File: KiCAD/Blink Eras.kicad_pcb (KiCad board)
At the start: 2 copper layers, 27.9 x 20.3 mm, 11 parts, among them IC1 ATTINY85-M, U1 ICM7555

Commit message: Hide passive component values.
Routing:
- net GND: track 2.79 -> 0.00 mm
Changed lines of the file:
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@@
     (thickness 1.6002)
     (drawings 8)
-    (tracks 73)
+    (tracks 71)
     (zones 0)
     (modules 11)
@@
   (page USLetter)
   (layers
-    (0 F.Cu signal hide)
+    (0 F.Cu signal)
     (31 B.Cu signal)
     (34 B.Paste user)
-    (35 F.Paste user hide)
+    (35 F.Paste user)
     (36 B.SilkS user)
-    (37 F.SilkS user hide)
+    (37 F.SilkS user)
     (38 B.Mask user)
-    (39 F.Mask user hide)
+    (39 F.Mask user)
     (44 Edge.Cuts user)
   )
@@
     (aux_axis_origin 0 0)
     (grid_origin 130.81 110.49)
-    (visible_elements FFFFFF7F)
+    (visible_elements FFFFFB7F)
     (pcbplotparams
       (layerselection 0x00030_80000001)
@@
       (effects (font (size 1 1) (thickness 0.15)))
     )
-    (fp_text value 1µ (at 0 1.9 270) (layer F.Fab)
+    (fp_text value 1µ (at 0 1.9 270) (layer F.Fab) hide
       (effects (font (size 1 1) (thickness 0.15)))
     )
@@
       (effects (font (size 1 1) (thickness 0.15)))
     )
-    (fp_text value Red (at 0 1.5 270) (layer F.Fab)
+    (fp_text value Red (at 0 1.5 270) (layer F.Fab) hide
       (effects (font (size 1 1) (thickness 0.15)))
     )
@@
       (effects (font (size 1 1) (thickness 0.15)))
     )
-    (fp_text value Green (at 0 1.5 270) (layer F.Fab)
+    (fp_text value Green (at 0 1.5 270) (layer F.Fab) hide
       (effects (font (size 1 1) (thickness 0.15)))
     )
@@
       (effects (font (size 1 1) (thickness 0.15)))
     )
-    (fp_text value 470K (at 0 1.9 90) (layer F.Fab)
+    (fp_text value 470K (at 0 1.9 90) (layer F.Fab) hide
       (effects (font (size 1 1) (thickness 0.15)))
     )
@@
       (effects (font (size 1 1) (thickness 0.15)))
     )
-    (fp_text value 68 (at 0 1.9 90) (layer F.Fab)
+    (fp_text value 68 (at 0 1.9 90) (layer F.Fab) hide
       (effects (font (size 1 1) (thickness 0.15)))
     )
@@
       (effects (font (size 1 1) (thickness 0.15)))
     )
-    (fp_text value 56 (at 0 1.9 270) (layer F.Fab)
+    (fp_text value 56 (at 0 1.9 270) (layer F.Fab) hide
       (effects (font (size 1 1) (thickness 0.15)))
     )
@@
   (segment (start 152.654 100.6) (end 155.31 100.6) (width 0.1524) (layer F.Cu) (net 1))
   (segment (start 155.31 100.6) (end 155.58 100.33) (width 0.1524) (layer F.Cu) (net 1))
-  (segment (start 144.78 100.33) (end 146.304 100.33) (width 0.1524) (layer B.Cu) (net 2))
-  (segment (start 146.304 100.33) (end 145.288 99.568) (width 0.1524) (layer B.Cu) (net 2))
   (via (at 145.288 99.568) (size 0.6858) (drill 0.3302) (layers F.Cu B.Cu) (net 2))
   (segment (start 137.16 107) (end 137.16 106.172) (width 0.1524) (layer F.Cu) (net 3))

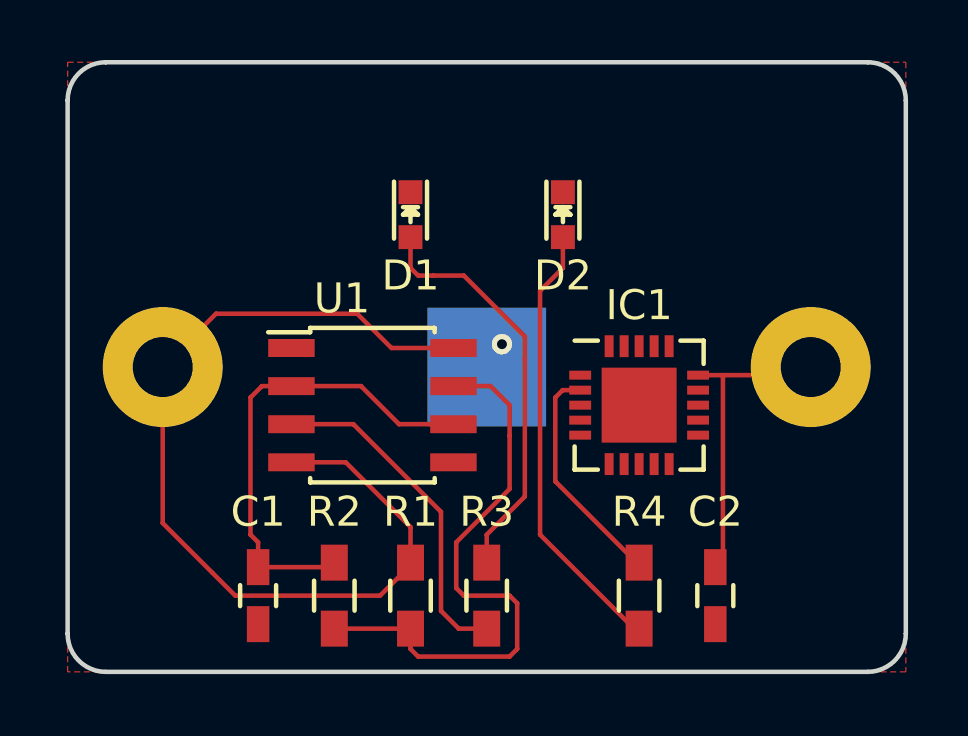
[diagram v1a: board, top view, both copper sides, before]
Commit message: New layout makes the pogo pins fit.
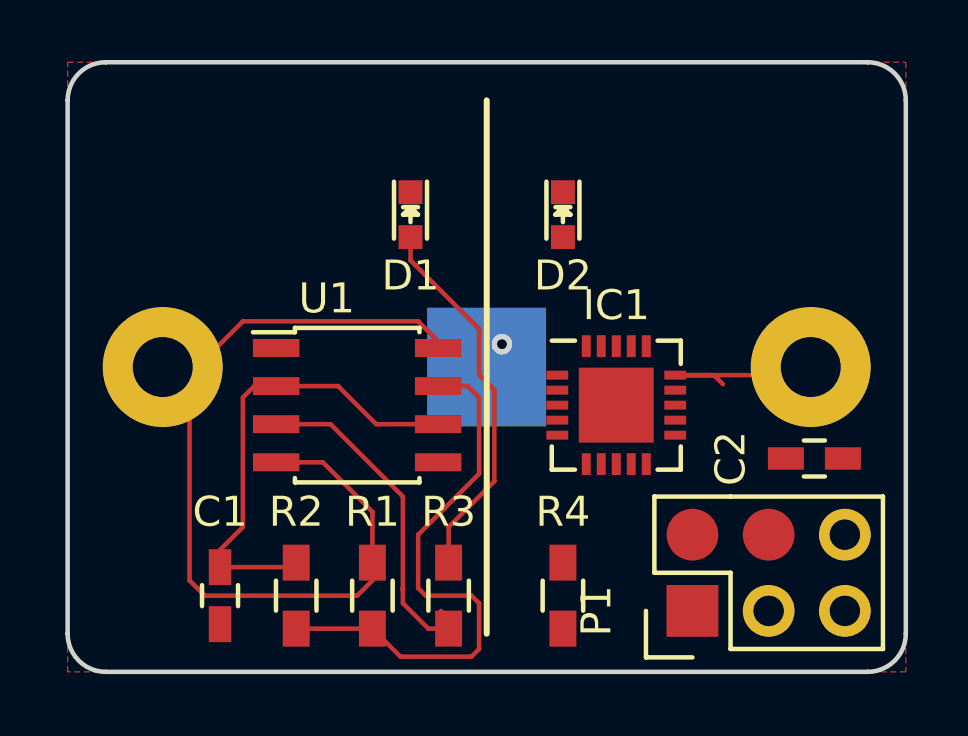
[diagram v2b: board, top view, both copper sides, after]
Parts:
- added P1: ISP, BlinkyFeet:ISP_Pogo_3-thru, F.Cu at (151.6, 108.5)
- moved C2 5.64 mm to (155.7, 103.4), turned to 0 degrees
- moved R4 2.54 mm to (147.3, 108.0)
- moved C1 1.27 mm to (135.9, 108.0)
- moved R1 1.27 mm to (141.0, 108.0)
- moved R3 1.27 mm to (143.5, 108.0)
- moved R2 1.27 mm to (138.4, 108.0)
- moved IC1 0.76 mm to (149.1, 101.6)
- moved U1 0.51 mm to (140.5, 101.6)
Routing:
- net Net-(D2-Pad2): track 14.8 -> 0.00 mm
- net Net-(IC1-Pad2): track 7.64 -> 0.07 mm
- net VCC: track 42.4 -> 37.0 mm
- net Net-(D1-Pad2): track 13.8 -> 12.6 mm
- net Net-(R1-Pad2): track 19.7 -> 19.1 mm
- net Net-(R3-Pad1): track 11.4 -> 12.1 mm

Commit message: Routed pogo pins.
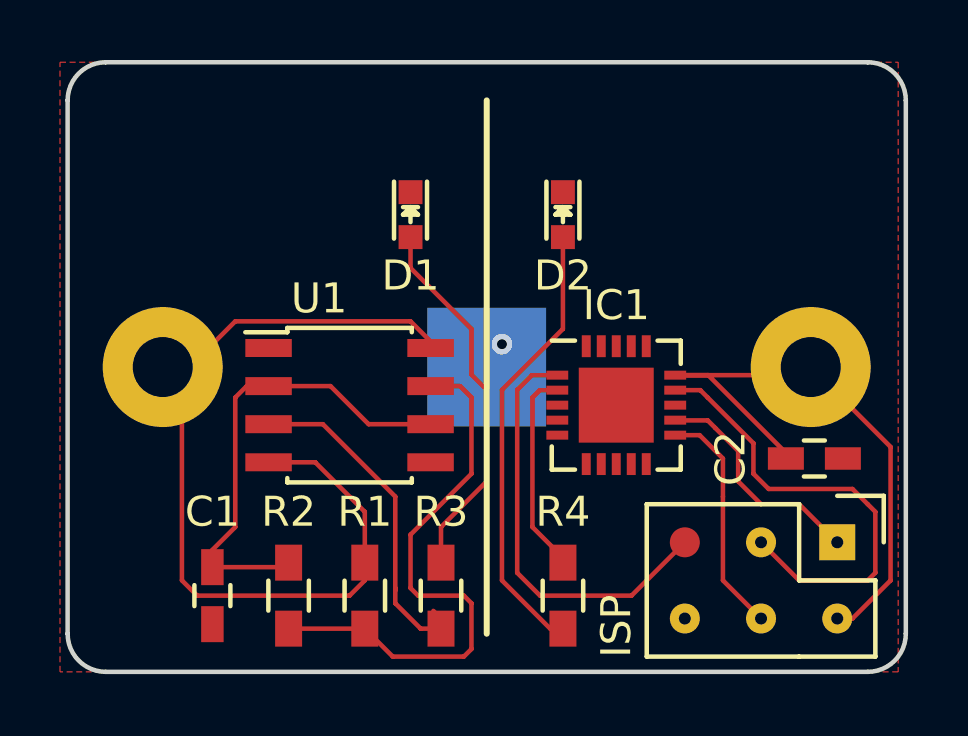
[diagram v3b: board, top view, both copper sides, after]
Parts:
- P1: footprint BlinkyFeet:ISP_Pogo_3-thru -> BlinkyFeet:ISP_Pogo_5-thru
- moved P1 5.34 mm to (156.5, 106.2), turned to 270 degrees
- moved R2 0.25 mm to (138.2, 108.0)
- moved C1 0.25 mm to (135.6, 108.0)
- moved R1 0.25 mm to (140.7, 108.0)
- moved R3 0.25 mm to (143.3, 108.0)
- moved U1 0.25 mm to (140.2, 101.6)
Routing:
- net /SCK: track 0.00 -> 15.4 mm
- net Net-(D2-Pad2): track 0.00 -> 15.0 mm
- net /~RESET~: track 0.00 -> 14.3 mm
- net VCC: track 37.0 -> 50.8 mm
- net /MISO: track 0.00 -> 7.95 mm
- net /MOSI: track 0.00 -> 7.77 mm
- net Net-(IC1-Pad2): track 0.07 -> 6.93 mm

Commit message: Tied QFN20's ground pad to ground.
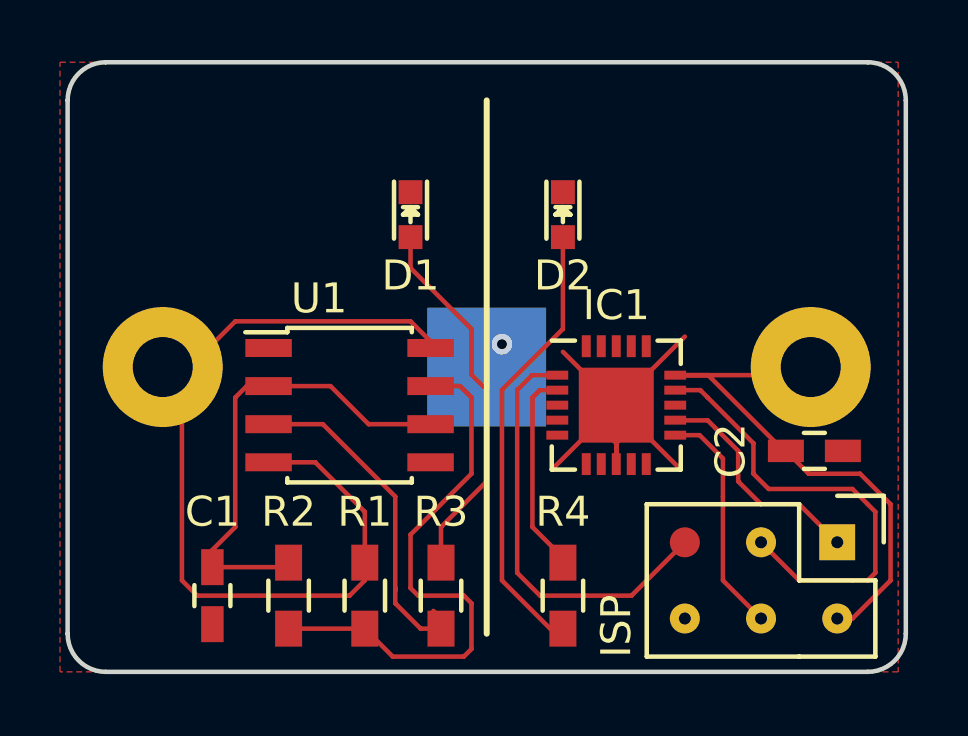
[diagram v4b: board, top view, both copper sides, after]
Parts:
- IC1: footprint Housings_DFN_QFN:QFN-20-1EP_4x4mm_Pitch0.5mm -> BlinkyFeet:QFN-20-1EP_4x4mm_Pitch0.5mm
- moved C2 0.25 mm to (155.7, 103.1)
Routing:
- net GND: track 0.00 -> 16.2 mm
- net VCC: track 50.8 -> 49.3 mm

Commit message: Big round battery contact, six vias to ground plane.
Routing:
- net GND: track 16.2 -> 60.8 mm, vias 1 -> 6
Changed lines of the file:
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@@
     (links 31)
     (no_connects 1)
-    (area 130.556 90.094999 158.825001 110.649401)
+    (area 130.556 90.0526 158.825001 110.649401)
     (thickness 1.6002)
     (drawings 9)
-    (tracks 129)
+    (tracks 153)
     (zones 0)
     (modules 12)
@@
     (add_net VCC)
   )
-  (module BlinkyFeet:BK-913 (layer B.Cu)
-    (at 144.78 100.33 180)
-    (fp_text reference BT1 (at 0 -8.89 180) (layer B.SilkS) hide
-      (effects (font (size 1 1) (thickness 0.15)) (justify mirror))
-    )
-    (fp_text value CR2032 (at 0 7.62 180) (layer B.SilkS)
-      (effects (font (size 1 1) (thickness 0.15)) (justify mirror))
-    )
-    (fp_circle (center 0 0) (end 10 0) (layer B.SilkS) (width 0.15))
-    (pad 1 thru_hole circle (at -10.8 0 180) (size 4 4) (drill 2) (layers *.Cu *.Mask B.SilkS)
-      (net 1 VCC))
-    (pad 2 smd rect (at 0 0 180) (size 3.96 3.96) (layers B.Cu B.Paste B.Mask)
-      (net 2 GND))
-    (pad 1 thru_hole circle (at 10.8 0 180) (size 4 4) (drill 2) (layers *.Cu *.Mask B.SilkS)
-      (net 1 VCC))
-    (model ${KIPRJMOD}/../FreeCAD/BK-913.wrl
-      (at (xyz 0 0 0.161417))
-      (scale (xyz 0.3937 0.3937 0.3937))
-      (rotate (xyz 0 0 0))
-    )
-  )
   (module Housings_SOIC:SOIC-8_3.9x4.9mm_Pitch1.27mm (layer F.Cu)
     (at 140.208 101.6)
@@
     (tags "SOIC 1.27")
     (attr smd)
-    (fp_text reference U1 (at -1.016 -3.556) (layer F.SilkS)
+    (fp_text reference U1 (at -4.826 1.778) (layer F.SilkS)
       (effects (font (size 1 1) (thickness 0.15)))
     )
@@
     (tags "QFN 0.5")
     (attr smd)
-    (fp_text reference IC1 (at 0 -3.33) (layer F.SilkS)
+    (fp_text reference IC1 (at 3.048 -1.27 90) (layer F.SilkS)
       (effects (font (size 1 1) (thickness 0.15)))
     )
@@
     )
   )
+  (module BlinkyFeet:BK-913 (layer B.Cu)
+    (at 144.78 100.33 180)
+    (fp_text reference BT1 (at 0 -8.89 180) (layer B.SilkS) hide
+      (effects (font (size 1 1) (thickness 0.15)) (justify mirror))
+    )
+    (fp_text value CR2032 (at 0 9.2 180) (layer B.SilkS)
+      (effects (font (size 1 1) (thickness 0.15)) (justify mirror))
+    )
+    (pad 1 thru_hole circle (at -10.8 0 180) (size 4 4) (drill 2) (layers *.Cu *.Mask B.SilkS)
+      (net 1 VCC))
+    (pad 2 smd circle (at 0 0 180) (size 17 17) (layers B.Cu B.Mask)
+      (net 2 GND))
+    (pad 1 thru_hole circle (at 10.8 0 180) (size 4 4) (drill 2) (layers *.Cu *.Mask B.SilkS)
+      (net 1 VCC))
+    (model ${KIPRJMOD}/../FreeCAD/BK-913.wrl
+      (at (xyz 0 0 0.161417))
+      (scale (xyz 0.3937 0.3937 0.3937))
+      (rotate (xyz 0 0 0))
+    )
+  )
   (gr_line (start 144.78 91.44) (end 144.78 109.22) (angle 90) (layer F.SilkS) (width 0.2))
   (gr_line (start 132.08 110.49) (end 157.48 110.49) (angle 90) (layer Edge.Cuts) (width 0.15))
@@
   (gr_arc (start 157.48 109.22) (end 158.75 109.22) (angle 90) (layer Edge.Cuts) (width 0.15))
   (gr_arc (start 157.48 91.44) (end 157.48 90.17) (angle 90) (layer Edge.Cuts) (width 0.15))
-  (segment (start 156.464 108.712) (end 156.972 108.712) (width 0.1524) (layer F.Cu) (net 1) (status 400000))
-  (segment (start 155.514 103.886) (end 154.752 103.124) (width 0.1524) (layer F.Cu) (net 1) (status 800000))
+  (segment (start 156.464 108.712) (end 156.972 108.712) (width 0.1524) (layer F.Cu) (net 1))
+  (segment (start 155.514 103.886) (end 154.752 103.124) (width 0.1524) (layer F.Cu) (net 1))
   (segment (start 157.226 103.886) (end 155.514 103.886) (width 0.1524) (layer F.Cu) (net 1))
   (segment (start 158.242 104.902) (end 157.226 103.886) (width 0.1524) (layer F.Cu) (net 1))
@@
   (segment (start 133.726 100.452) (end 133.726 100.33) (width 0.1524) (layer F.Cu) (net 1))
   (segment (start 151.063 100.6) (end 155.31 100.6) (width 0.1524) (layer F.Cu) (net 1))
+  (segment (start 137.508 99.695) (end 139.319 99.695) (width 0.1524) (layer F.Cu) (net 2))
+  (segment (start 139.446 99.822) (end 139.954 100.33) (width 0.1524) (layer B.Cu) (net 2))
+  (via (at 139.446 99.822) (size 0.6858) (drill 0.3302) (layers F.Cu B.Cu) (net 2))
+  (segment (start 139.319 99.695) (end 139.446 99.822) (width 0.1524) (layer F.Cu) (net 2))
+  (segment (start 139.954 100.33) (end 144.78 100.33) (width 0.1524) (layer B.Cu) (net 2))
+  (segment (start 151.384 99.314) (end 151.13 99.568) (width 0.1524) (layer F.Cu) (net 2))
+  (segment (start 149.723 100.975) (end 151.384 99.314) (width 0.1524) (layer F.Cu) (net 2))
+  (segment (start 151.13 99.568) (end 150.368 100.33) (width 0.1524) (layer B.Cu) (net 2))
+  (via (at 151.13 99.568) (size 0.6858) (drill 0.3302) (layers F.Cu B.Cu) (net 2))
+  (segment (start 150.368 100.33) (end 144.78 100.33) (width 0.1524) (layer B.Cu) (net 2))
+  (via (at 147.066 103.632) (size 0.6858) (drill 0.3302) (layers F.Cu B.Cu) (net 2))
+  (segment (start 147.066 103.632) (end 144.78 101.346) (width 0.1524) (layer B.Cu) (net 2))
+  (segment (start 144.78 101.346) (end 144.78 100.33) (width 0.1524) (layer B.Cu) (net 2))
+  (via (at 151.13 103.632) (size 0.6858) (drill 0.3302) (layers F.Cu B.Cu) (net 2))
+  (segment (start 151.13 103.632) (end 147.828 100.33) (width 0.1524) (layer B.Cu) (net 2))
+  (segment (start 147.828 100.33) (end 144.78 100.33) (width 0.1524) (layer B.Cu) (net 2))
+  (segment (start 147.32 94.5007) (end 148.8313 94.5007) (width 0.1524) (layer F.Cu) (net 2))
+  (segment (start 148.844 94.488) (end 144.78 98.552) (width 0.1524) (layer B.Cu) (net 2))
+  (via (at 148.844 94.488) (size 0.6858) (drill 0.3302) (layers F.Cu B.Cu) (net 2))
+  (segment (start 148.8313 94.5007) (end 148.844 94.488) (width 0.1524) (layer F.Cu) (net 2))
+  (segment (start 144.78 98.552) (end 144.78 100.33) (width 0.1524) (layer B.Cu) (net 2))
+  (segment (start 142.24 94.5007) (end 140.7287 94.5007) (width 0.1524) (layer F.Cu) (net 2))
+  (segment (start 140.716 94.488) (end 144.78 98.552) (width 0.1524) (layer B.Cu) (net 2))
+  (via (at 140.716 94.488) (size 0.6858) (drill 0.3302) (layers F.Cu B.Cu) (net 2))
+  (segment (start 140.7287 94.5007) (end 140.716 94.488) (width 0.1524) (layer F.Cu) (net 2))
+  (segment (start 144.78 98.552) (end 144.78 100.33) (width 0.1524) (layer B.Cu) (net 2))
   (segment (start 149.723 102.225) (end 151.13 103.632) (width 0.1524) (layer F.Cu) (net 2))
   (segment (start 148.473 102.225) (end 147.066 103.632) (width 0.1524) (layer F.Cu) (net 2))
   (segment (start 148.473 100.975) (end 147.32 99.822) (width 0.1524) (layer F.Cu) (net 2))
-  (segment (start 149.723 100.975) (end 151.384 99.314) (width 0.1524) (layer F.Cu) (net 2))
   (segment (start 149.723 100.975) (end 149.723 102.225) (width 0.1524) (layer F.Cu) (net 2))
   (segment (start 149.723 102.225) (end 149.723 102.245) (width 0.1524) (layer F.Cu) (net 2))
@@
   (segment (start 148.473 100.975) (end 148.473 102.225) (width 0.1524) (layer F.Cu) (net 2))
   (segment (start 149.723 100.975) (end 148.473 100.975) (width 0.1524) (layer F.Cu) (net 2))
-  (via (at 145.288 99.568) (size 0.6858) (drill 0.3302) (layers F.Cu B.Cu) (net 2))
   (segment (start 137.508 100.965) (end 139.573 100.965) (width 0.1524) (layer F.Cu) (net 3))
   (segment (start 140.843 102.235) (end 142.908 102.235) (width 0.1524) (layer F.Cu) (net 3))

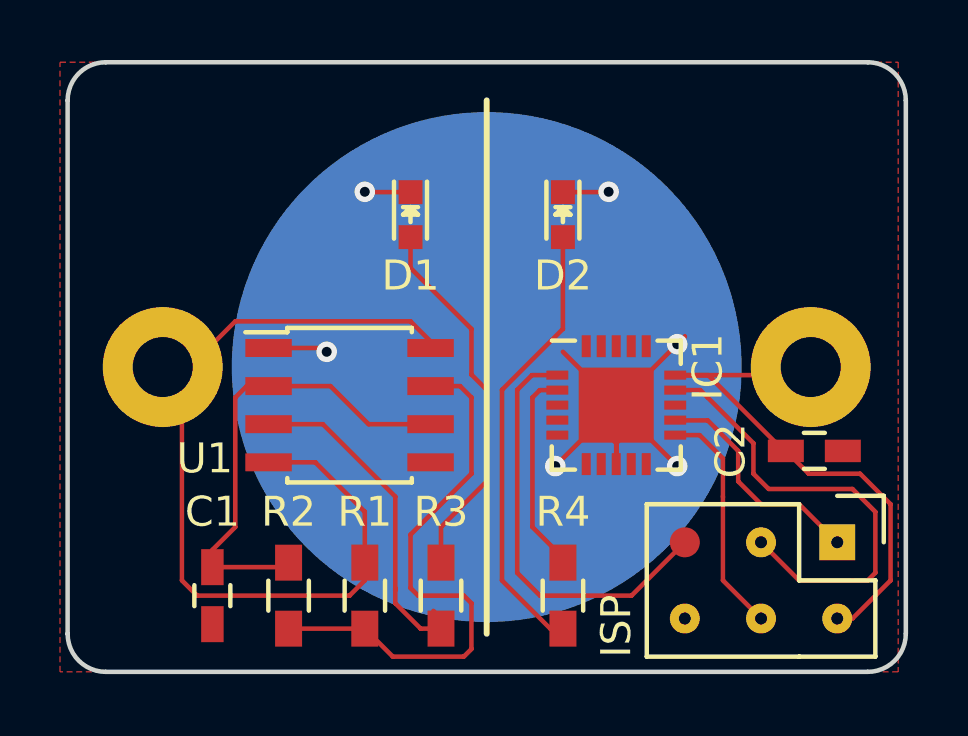
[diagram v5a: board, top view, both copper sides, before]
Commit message: Moved ATtiny bypass cap.
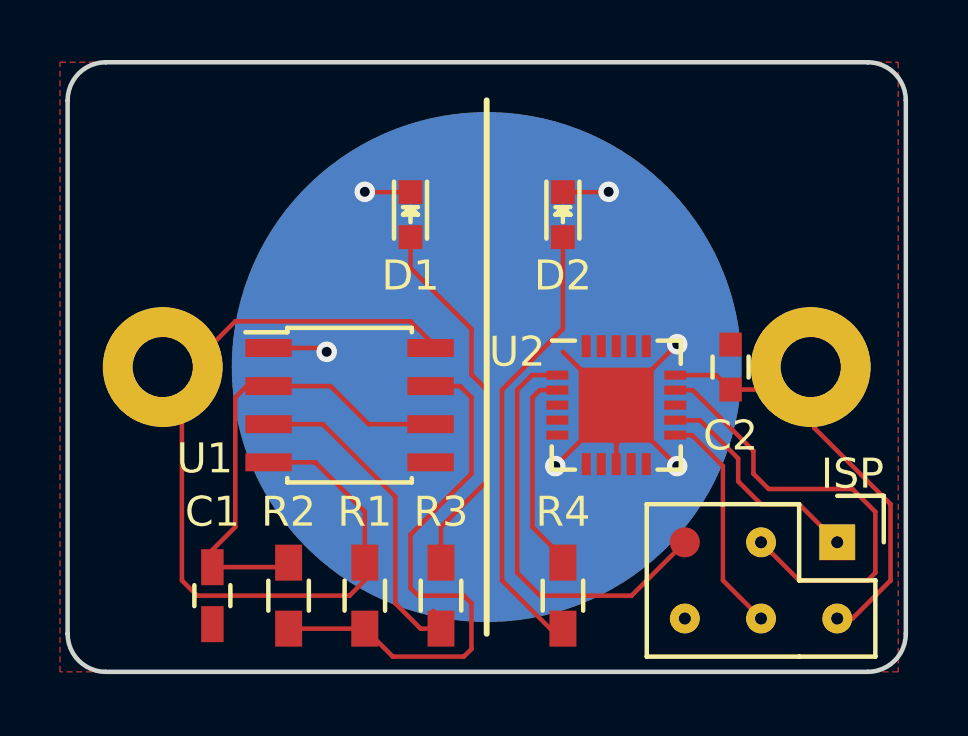
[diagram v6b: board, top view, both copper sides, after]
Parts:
- C2: footprint Capacitors_SMD:C_0603_HandSoldering -> Capacitors_SMD:C_0603
- moved C2 3.95 mm to (152.9, 100.3), turned to 90 degrees
- renumbered IC1 to U2
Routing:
- net VCC: track 49.3 -> 46.6 mm
- net GND: track 60.8 -> 59.4 mm
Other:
- rule pad_to_mask_clearance: 0.2 -> 0.05

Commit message: Cleaned up extraneous traces inside pads.
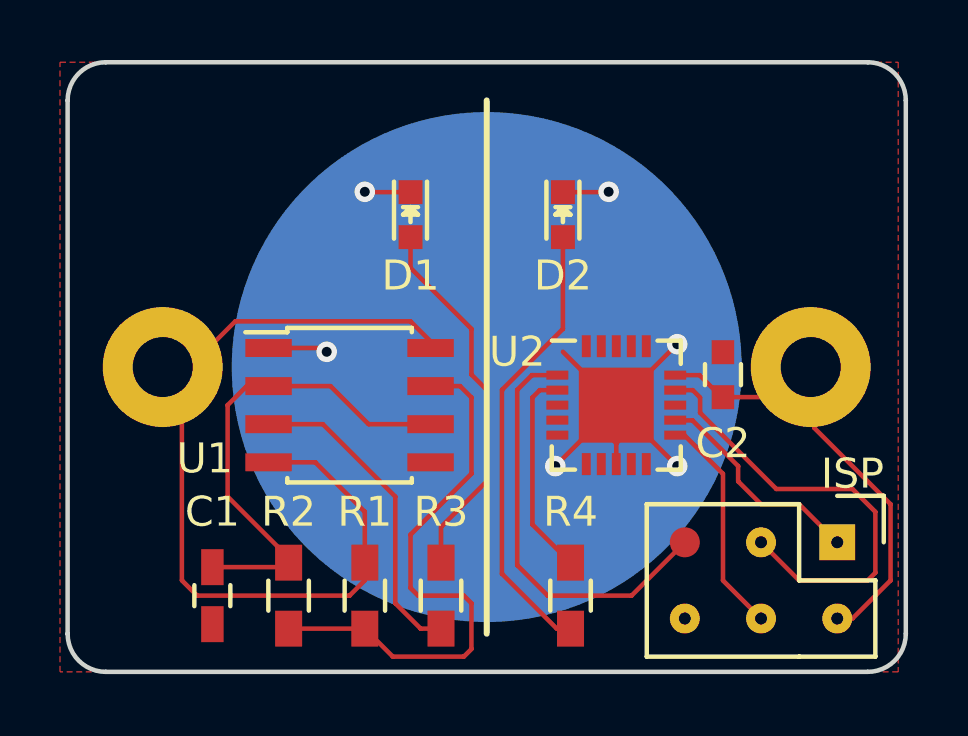
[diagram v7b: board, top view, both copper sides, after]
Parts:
- moved C2 0.36 mm to (152.7, 100.6)
- moved R4 0.25 mm to (147.6, 108.0)
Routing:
- net Net-(R3-Pad1): track 12.0 -> 10.7 mm
